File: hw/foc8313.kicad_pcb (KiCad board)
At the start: 4 copper layers, 35 x 35 mm, 99 parts, among them J1 Tag Connect, J2 Encoder, J3 CAN, J4 CAN, J6 GPIO, SW1 SW_SPST, SW2 SW_SPST, U1 LMR36015SFBRNXR, U12 TJA1051TK/3,118, U2 XC6206P332MR, U3 DRV8313PWP, U4 STM32F103CBTx, U5 AS5047D, U6 ZD24C08AE1-STGMT, U7 INA240A2D, U8 INA240A2D, X1 X322516MLB4SI

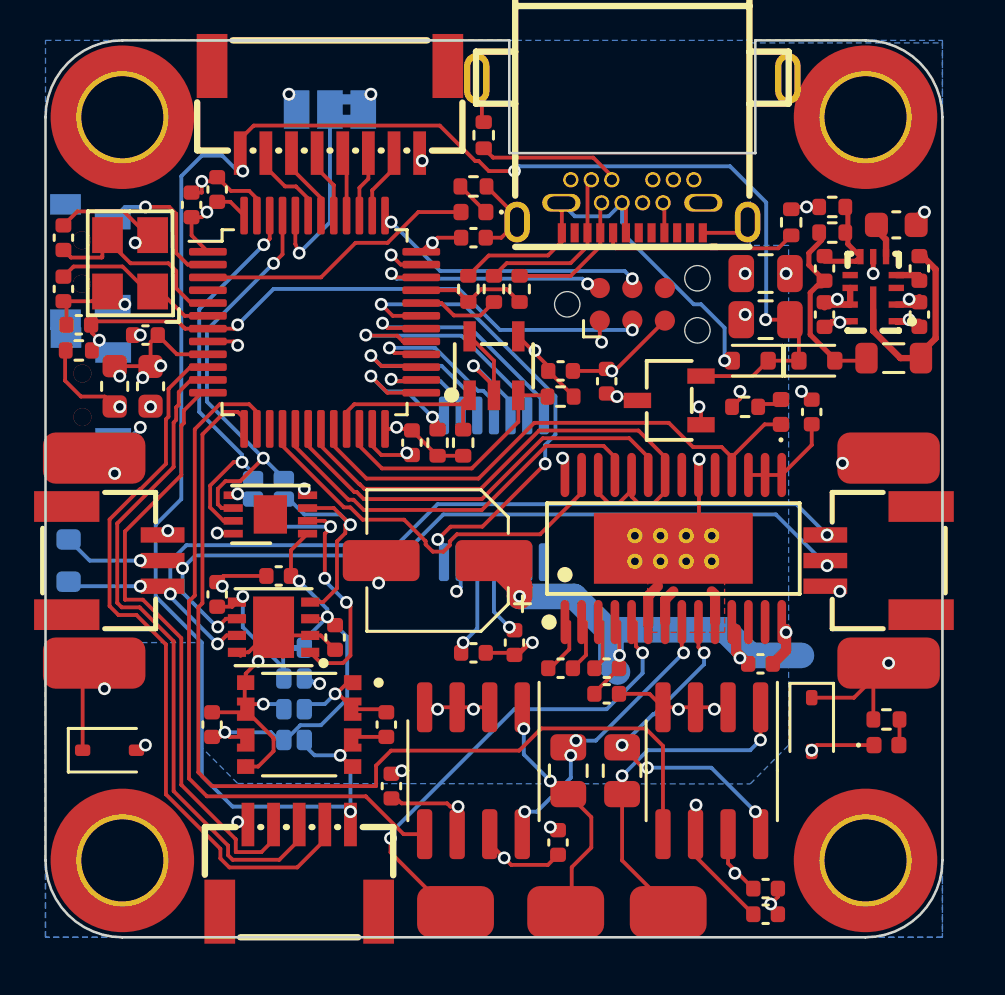
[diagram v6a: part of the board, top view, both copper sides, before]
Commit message: [Hw] Aligned DRV IC, thick power traces
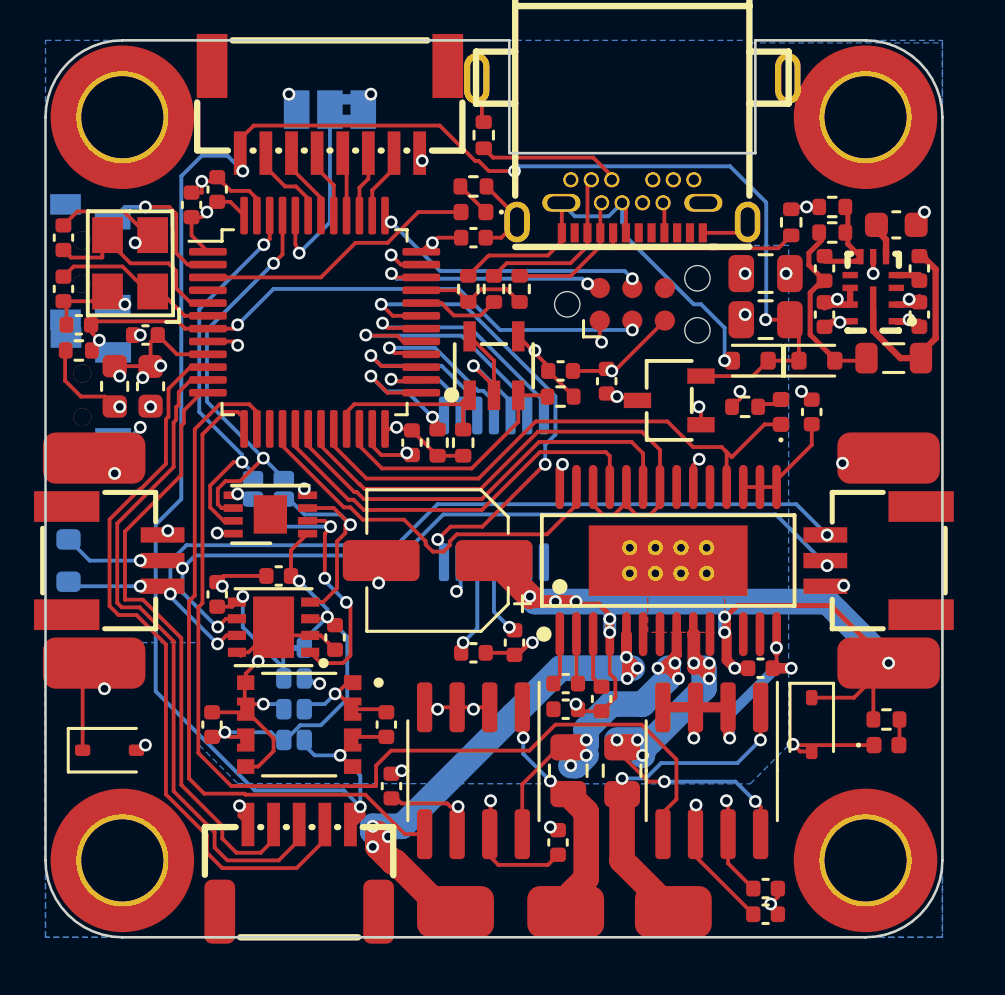
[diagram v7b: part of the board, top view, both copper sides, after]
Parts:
- moved C20 1.71 mm to (142.8, 108.6), turned to 180 degrees
- moved C22 1.22 mm to (144.2, 108.2), turned to 90 degrees
- moved C23 0.63 mm to (142.8, 107.6)
- moved U3 0.51 mm to (146.8, 102.8)
- moved H9 0.20 mm to (147.0, 116.5)
- moved C21 0.17 mm to (150.4, 107.0)
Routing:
- net VCC: track 33.1 -> 51.3 mm, vias 8 -> 14
- net /PHC: track 12.6 -> 19.5 mm, vias 4 -> 8
- net /PHB: track 9.90 -> 15.0 mm, vias 4 -> 6
- net +3.3VA: track 11.2 -> 14.0 mm
- net GND: track 69.7 -> 72.2 mm, vias 42 -> 43
- net /OUTA: track 18.8 -> 21.3 mm, vias 2 -> 6
- net /OUTB: track 7.76 -> 9.37 mm
- net /~{DRV_NFAULT}: track 21.3 -> 22.1 mm
- net /~{DRV_NRST}: track 3.76 -> 4.32 mm

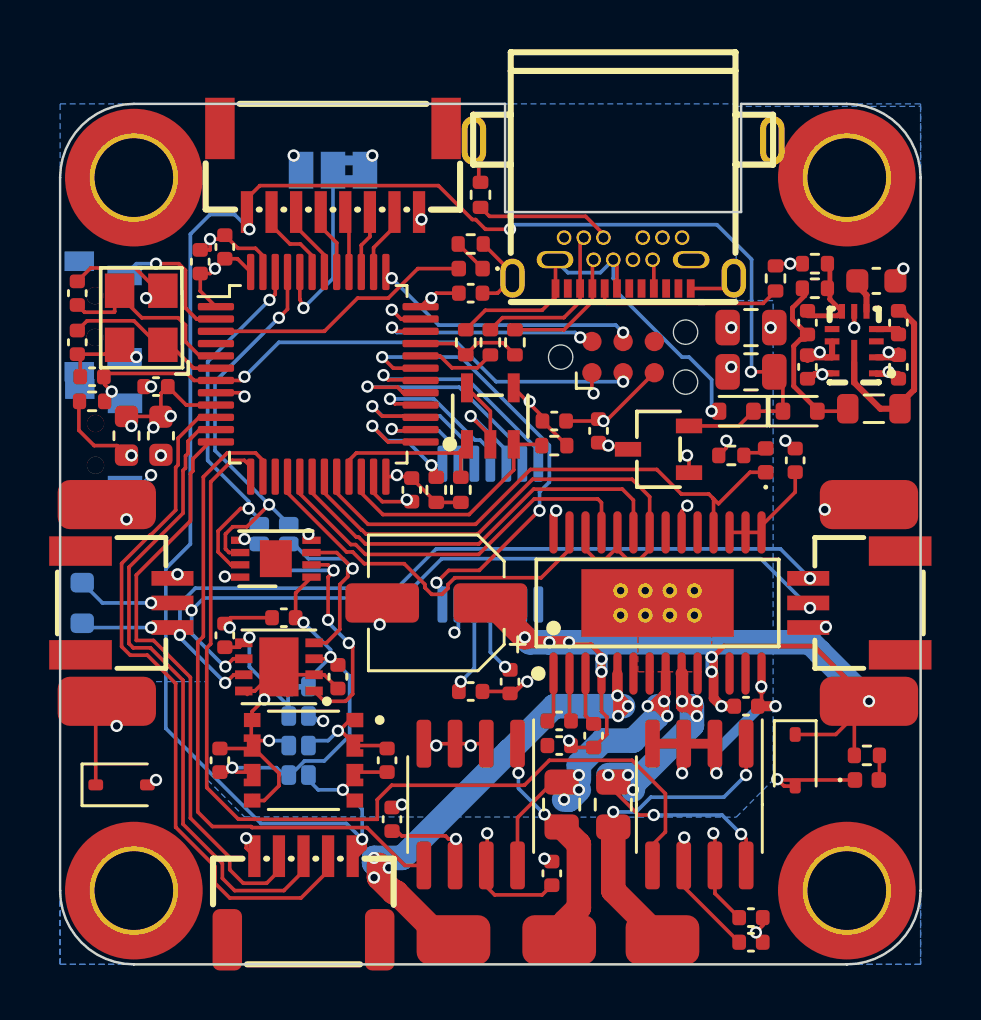
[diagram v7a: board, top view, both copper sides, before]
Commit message: [Hw] Added labels to silkscreen
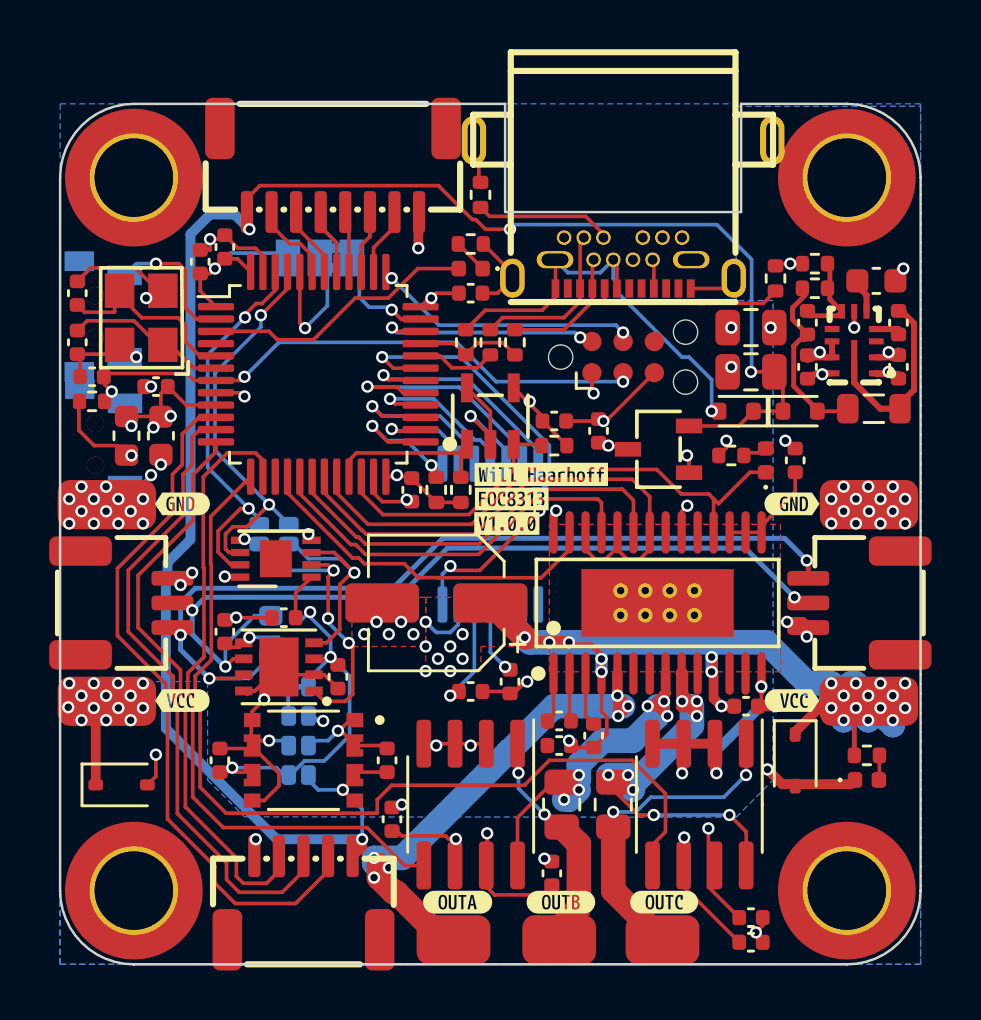
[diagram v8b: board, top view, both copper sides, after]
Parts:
- added kibuzzard-6635905B: G***, kibuzzard-6635905B, B.Cu at (155.9, 101.8)
- added kibuzzard-6635906D: G***, kibuzzard-6635906D, B.Cu at (155.9, 102.8)
- added kibuzzard-66359090: G***, kibuzzard-66359090, B.Cu at (155.5, 103.8)
- added kibuzzard-663591A5: G***, kibuzzard-663591A5, B.Cu at (124.5, 101.8)
- added kibuzzard-663591BC: G***, kibuzzard-663591BC, B.Cu at (124.1, 102.8)
- added kibuzzard-663591C6: G***, kibuzzard-663591C6, B.Cu at (124.1, 103.8)
- added kibuzzard-6635923C: G***, kibuzzard-6635923C, B.Cu at (130.5, 116.0)
- added kibuzzard-6635923C: G***, kibuzzard-6635923C, B.Cu at (134.3, 91.0)
- added kibuzzard-6635923C: G***, kibuzzard-6635923C, B.Cu at (134.5, 108.6)
- added kibuzzard-6635923C: G***, kibuzzard-6635923C, B.Cu at (137.1, 84.0)
- added kibuzzard-6635926F: G***, kibuzzard-6635926F, B.Cu at (133.1, 91.4)
- added kibuzzard-66359297: G***, kibuzzard-66359297, B.Cu at (134.5, 107.4)
- added kibuzzard-66359297: G***, kibuzzard-66359297, B.Cu at (131.9, 91.0)
- added kibuzzard-663592D6: G***, kibuzzard-663592D6, B.Cu at (134.5, 116.2)
- added kibuzzard-663592D6: G***, kibuzzard-663592D6, B.Cu at (134.3, 109.8)
- added kibuzzard-663592D6: G***, kibuzzard-663592D6, B.Cu at (130.1, 83.8)
- added kibuzzard-66359322: G***, kibuzzard-66359322, B.Cu at (131.1, 84.0)
- added kibuzzard-66359333: G***, kibuzzard-66359333, B.Cu at (132.1, 84.0)
- added kibuzzard-6635934E: G***, kibuzzard-6635934E, B.Cu at (133.1, 84.0)
- added kibuzzard-66359356: G***, kibuzzard-66359356, B.Cu at (134.1, 84.0)
- added kibuzzard-6635935F: G***, kibuzzard-6635935F, B.Cu at (135.1, 84.0)
- added kibuzzard-66359375: G***, kibuzzard-66359375, B.Cu at (136.1, 84.2)
- added kibuzzard-6635961B: G***, kibuzzard-6635961B, B.Cu at (127.5, 91.4)
- added kibuzzard-66359642: G***, kibuzzard-66359642, B.Cu at (127.7, 96.2)
- added kibuzzard-663596D7: G***, kibuzzard-663596D7, B.Cu at (134.9, 106.2)
- added kibuzzard-66359707: G***, kibuzzard-66359707, B.Cu at (134.1, 99.6)
- added kibuzzard-6635971B: G***, kibuzzard-6635971B, B.Cu at (134.1, 100.6)
- added kibuzzard-6635973B: G***, kibuzzard-6635973B, B.Cu at (128.3, 99.6)
- added kibuzzard-6635974A: G***, kibuzzard-6635974A, B.Cu at (128.3, 100.6)
- added kibuzzard-66359780: G***, kibuzzard-66359780, B.Cu at (129.5, 107.4)
- added kibuzzard-66359780: G***, kibuzzard-66359780, B.Cu at (129.5, 106.2)
- added kibuzzard-66359792: G***, kibuzzard-66359792, B.Cu at (129.5, 108.6)
- added kibuzzard-663597E2: G***, kibuzzard-663597E2, B.Cu at (129.5, 109.8)
- added kibuzzard-6635988E: G***, kibuzzard-6635988E, B.Cu at (146.9, 115.8)
- added kibuzzard-663598FD: G***, kibuzzard-663598FD, B.Cu at (132.1, 104.2)
- added kibuzzard-663599A9: G***, kibuzzard-663599A9, B.Cu at (138.5, 115.8)
- added kibuzzard-663599B0: G***, kibuzzard-663599B0, B.Cu at (142.7, 115.8)
- added kibuzzard-66359A05: G***, kibuzzard-66359A05, F.Cu at (138.7, 115.0)
- added kibuzzard-66359A1C: G***, kibuzzard-66359A1C, F.Cu at (142.9, 115.0)
- added kibuzzard-66359A28: G***, kibuzzard-66359A28, F.Cu at (147.1, 115.0)
- added kibuzzard-66359A50: G***, kibuzzard-66359A50, F.Cu at (127.5, 106.8)
- added kibuzzard-66359A77: G***, kibuzzard-66359A77, F.Cu at (127.5, 98.8)
- added kibuzzard-66359A9E: G***, kibuzzard-66359A9E, F.Cu at (152.3, 106.8)
- added kibuzzard-66359AB0: G***, kibuzzard-66359AB0, F.Cu at (152.3, 98.8)
- added kibuzzard-66359AE4: G***, kibuzzard-66359AE4, F.Cu at (140.9, 98.6)
- added kibuzzard-66359B17: G***, kibuzzard-66359B17, F.Cu at (142.1, 97.6)
- added kibuzzard-66359B89: G***, kibuzzard-66359B89, F.Cu at (140.7, 99.6)
- moved R2 7.79 mm to (131.1, 104.1)
- moved JP1 3.61 mm to (133.1, 88.8)
- moved C34 0.15 mm to (129.2, 104.0)
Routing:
- net GND: track 72.2 -> 80.1 mm, vias 43 -> 71
- net +3.3V: track 32.2 -> 35.7 mm, vias 13 -> 12
- net /BOOT0: track 7.59 -> 5.80 mm
- net /ISENSE_C: track 39.4 -> 37.9 mm
- net /CAN.H: track 35.2 -> 36.5 mm, vias 4 -> 3
- net /CAN.GND: track 18.8 -> 20.0 mm, vias 6 -> 8
- net VCC: track 51.3 -> 52.5 mm, vias 14 -> 47
- net /CAN.L: track 33.9 -> 35.0 mm, vias 4 -> 3
- net /isocan/ISO5V: track 17.3 -> 18.0 mm
- net Net-(U5-VDD3V3): track 3.37 -> 4.11 mm
- net /DRV_INA: track 15.5 -> 14.7 mm
- net /ENC2_Z: track 23.9 -> 23.3 mm
- added copper zone on F.Cu, net GND
- added copper zone on F.Cu, net VCC
- removed copper zone on F.Cu, net +3V3
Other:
- board text added: "Version 1.0.0"
- board text added: "Will Haarhoff"
- board text added: "foc8313"
